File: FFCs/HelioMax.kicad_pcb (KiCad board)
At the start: 2 copper layers, 252.5 x 156.3 mm, 77 parts, among them J1 Conn_01x01_Pin, J10 Conn_01x07, J11 Conn_01x07, J12 Conn_Telorum_Belt, J13 Conn_to_Telorum_Belt, J4 Conn_C_to_Praetor_Enclave, J5 Conn_R_to_Praetor_Enclave, J6 Conn_01x07, J7 Conn_01x07, J8 Conn_to_Pollex_Cluster, J9 Conn_Pollex_Cluster, SW0:10 SW0:3, SW0:11 SW0:2, SW0:12 SW0:1, SW0:7 SW0:6, SW0:8 SW0:5, SW0:9 SW0:4, SW1:10 SW1:3, SW1:11 SW1:2, SW1:12 SW1:1, SW1:13 SW1:0, SW1:9 SW1:4, SW2:10 SW2:3, SW2:11 SW2:2, SW2:12 SW2:1, SW2:13 SW2:0, SW2:7 SW2:6, SW2:8 SW2:5, SW2:9 SW2:4, SW3:10 SW3:3, SW3:11 SW3:2, SW3:12 SW3:1, SW3:13 SW3:0, SW3:8 SW3:5, SW3:9 SW3:4, SW4:10 SW4:3, SW4:11 SW4:2, SW4:12 SW4:1, SW4:13 SW4:0, SW4:7 SW4:6, SW4:8 SW4:5, SW4:9 SW4:4, SW5:10 SW5:3, SW5:11 SW5:2, SW5:12 SW5:1, SW5:13 SW5:0, SW5:7 SW5:6, SW5:8 SW5:5, SW5:9 SW5:4, SW6:10 SW6:3, SW6:11 SW6:2, SW6:12 SW6:1, SW6:13 SW6:0, SW6:7 SW6:6, SW6:8 SW6:5, SW6:9 SW6:4

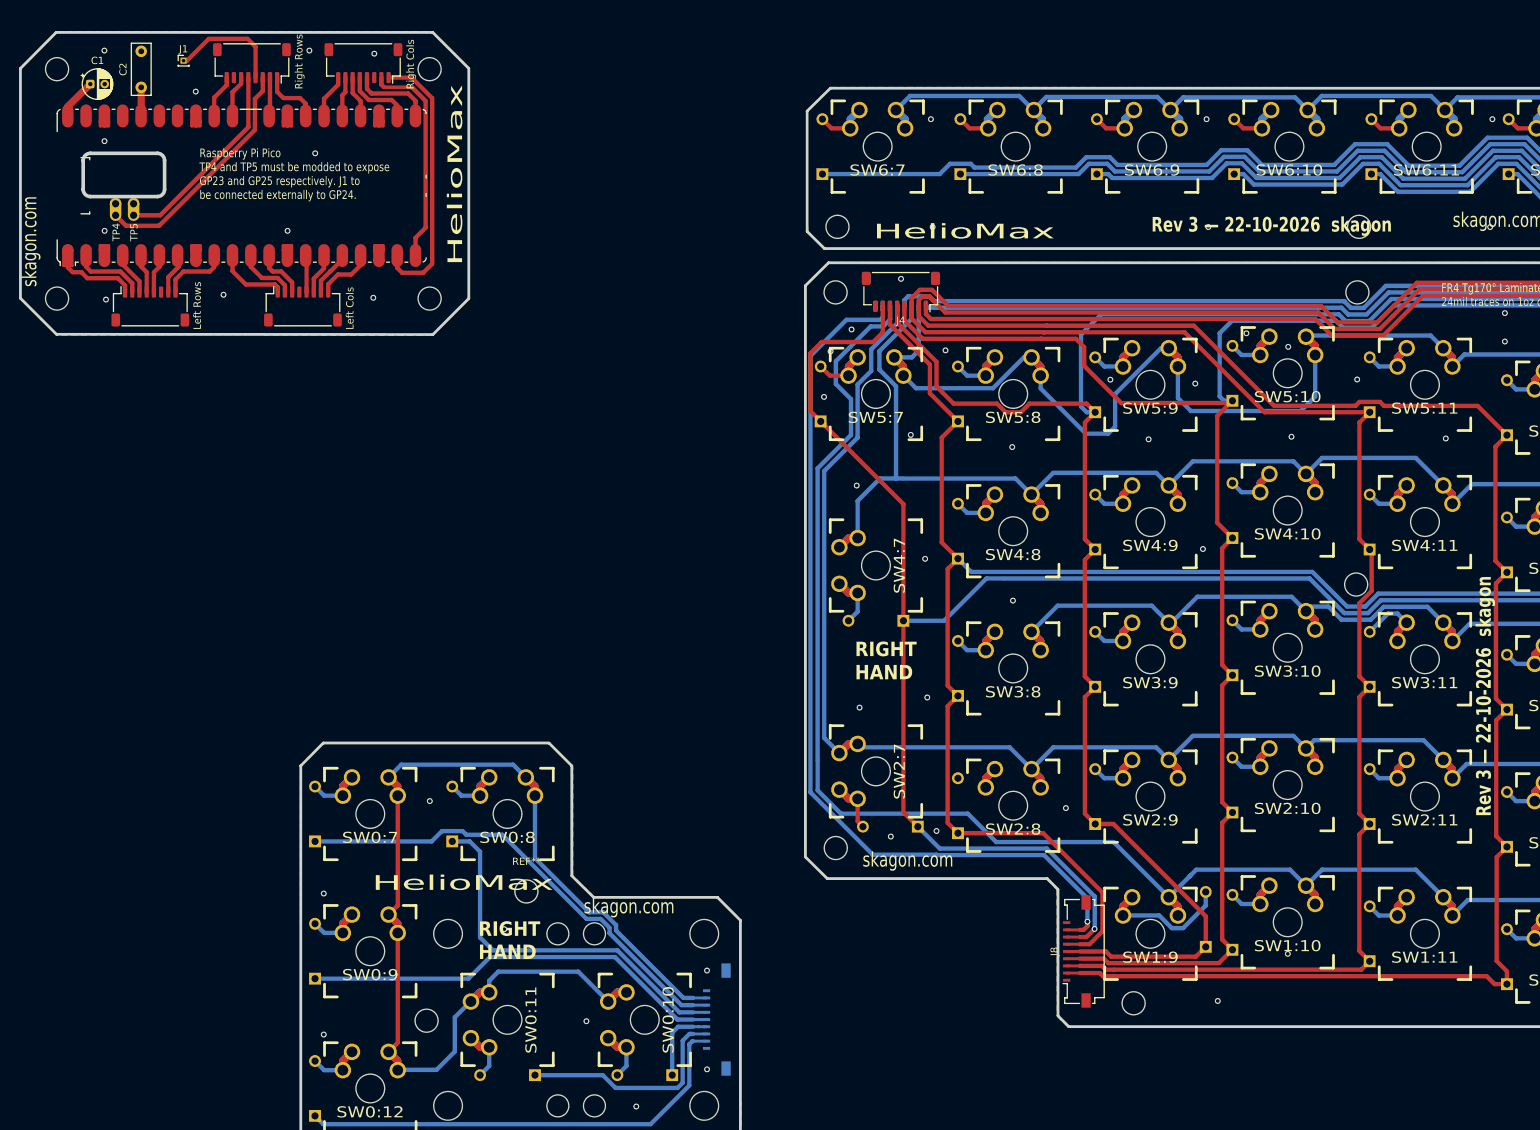
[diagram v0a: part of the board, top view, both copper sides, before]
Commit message: Fixed FFC connector, grounded the MPs.
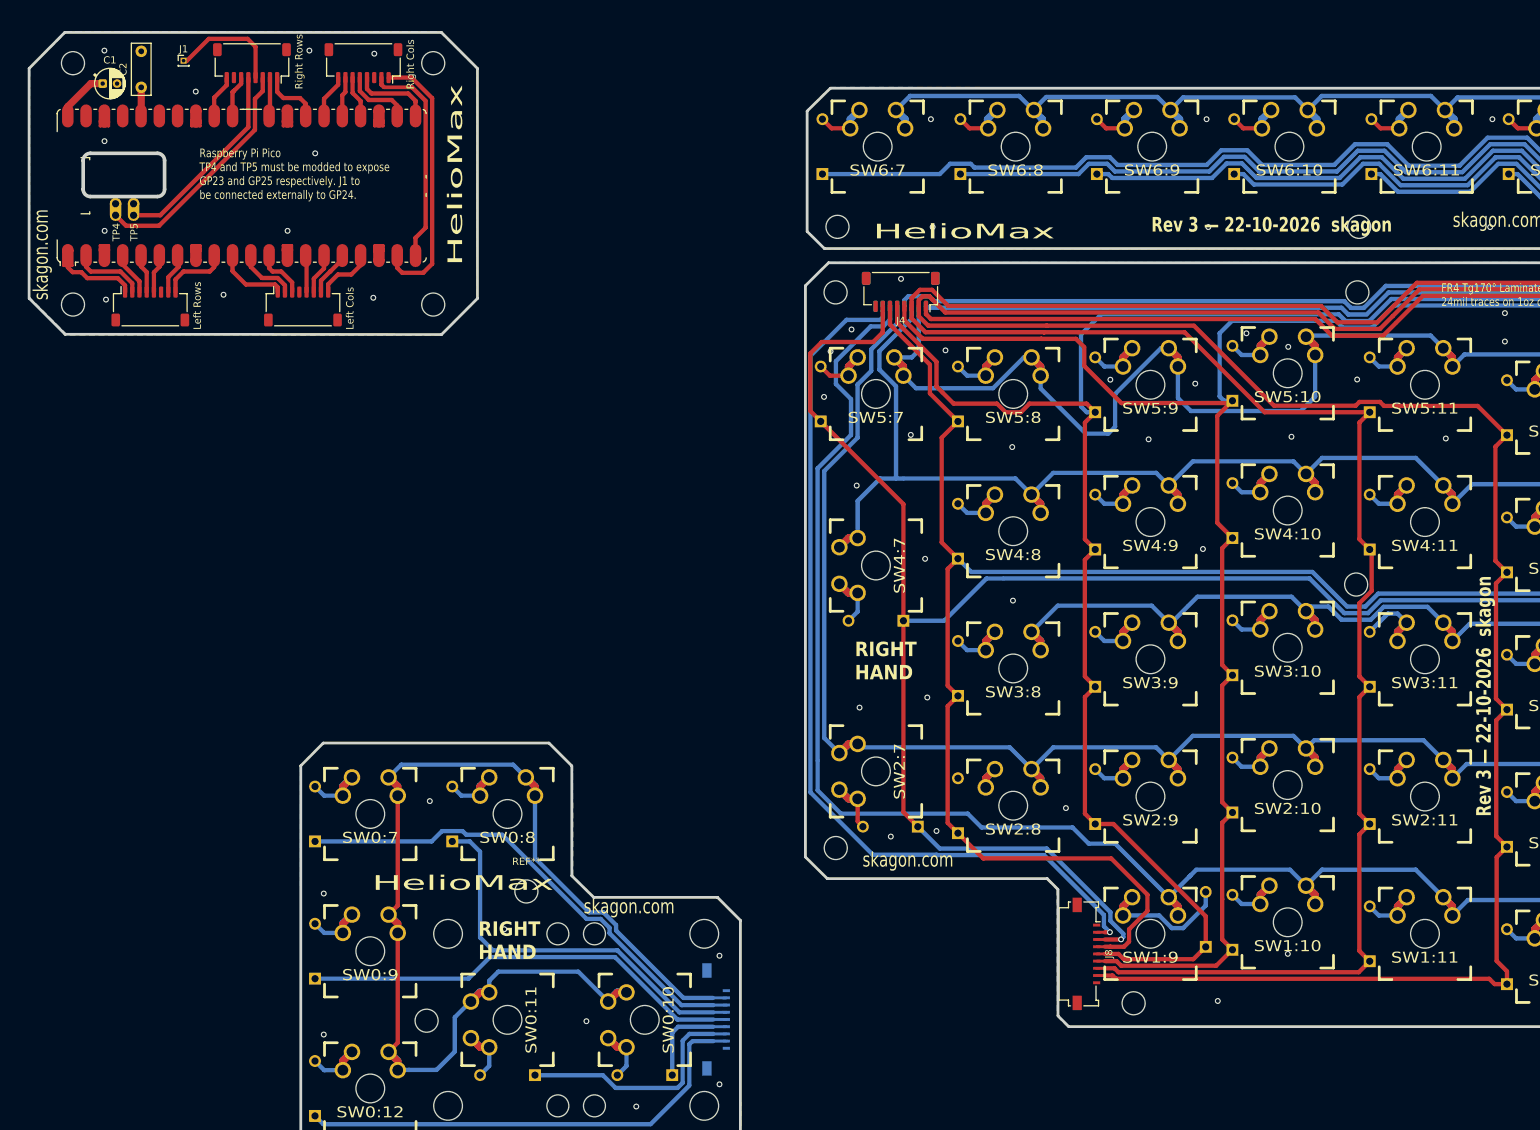
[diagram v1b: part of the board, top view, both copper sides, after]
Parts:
- moved J8 2.37 mm to (169.9, 152.0), turned to -90 degrees
- moved H12 2.36 mm to (28.8, 28.4)
- moved H13 2.36 mm to (28.8, 61.9)
- moved C1 1.72 mm to (32.9, 31.2)
- moved H14 0.97 mm to (78.8, 61.9)
- moved REF** 0.97 mm to (78.8, 28.4)
- moved J9 0.92 mm to (118.5, 161.1), turned to 90 degrees
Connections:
- J12 pad MP: (no net) -> GND
- J13 pad MP: (no net) -> GND
- J4 pad MP: (no net) -> GND
- J5 pad MP: (no net) -> GND
- J8 pad 2: /COL1 -> /ROW0
- J8 pad 3: /COL2 -> /COL6
- J8 pad 4: /COL3 -> /COL5
- J8 pad 6: /COL5 -> /COL3
- J8 pad 7: /COL6 -> /COL2
- J8 pad 8: /ROW0 -> /COL1
- J8 pad MP: (no net) -> GND
- J9 pad 2: /ROW0 -> /COL1
- J9 pad 3: /COL6 -> /COL2
- J9 pad 4: /COL5 -> /COL3
- J9 pad 6: /COL3 -> /COL5
- J9 pad 7: /COL2 -> /COL6
- J9 pad 8: /COL1 -> /ROW0
- J9 pad MP: (no net) -> GND
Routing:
- net /COL5: track 469.0 -> 479.2 mm
- net /COL6: track 524.4 -> 529.5 mm
- net /ROW0: track 346.5 -> 350.0 mm
- net Net-(A1-VBUS): track 6.51 -> 8.26 mm
- net /COL1: track 462.1 -> 460.5 mm
- net /COL4: track 444.5 -> 443.3 mm
- net /COL3: track 355.1 -> 354.0 mm
- net /COL2: track 443.7 -> 442.6 mm
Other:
- board size 252.5 x 156.3 mm -> 251.3 x 156.3 mm
